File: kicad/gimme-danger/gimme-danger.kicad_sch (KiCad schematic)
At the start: 59 parts, among them J2 Barrel_Jack, J3 Screw_Terminal_01x06, Q1 AO3400A, Q2 AO3400A, Q3 AO3400A, Q4 AO3400A, U1 ESP32-S3-WROOM-1, U2 TPD6S300RUKR, U3 U261-241N-4BS2SS, U4 AO4407A, U5 SKRKAEE020, U6 DDTC143EUA, U7 SKRKAEE020, U8 TPS54302

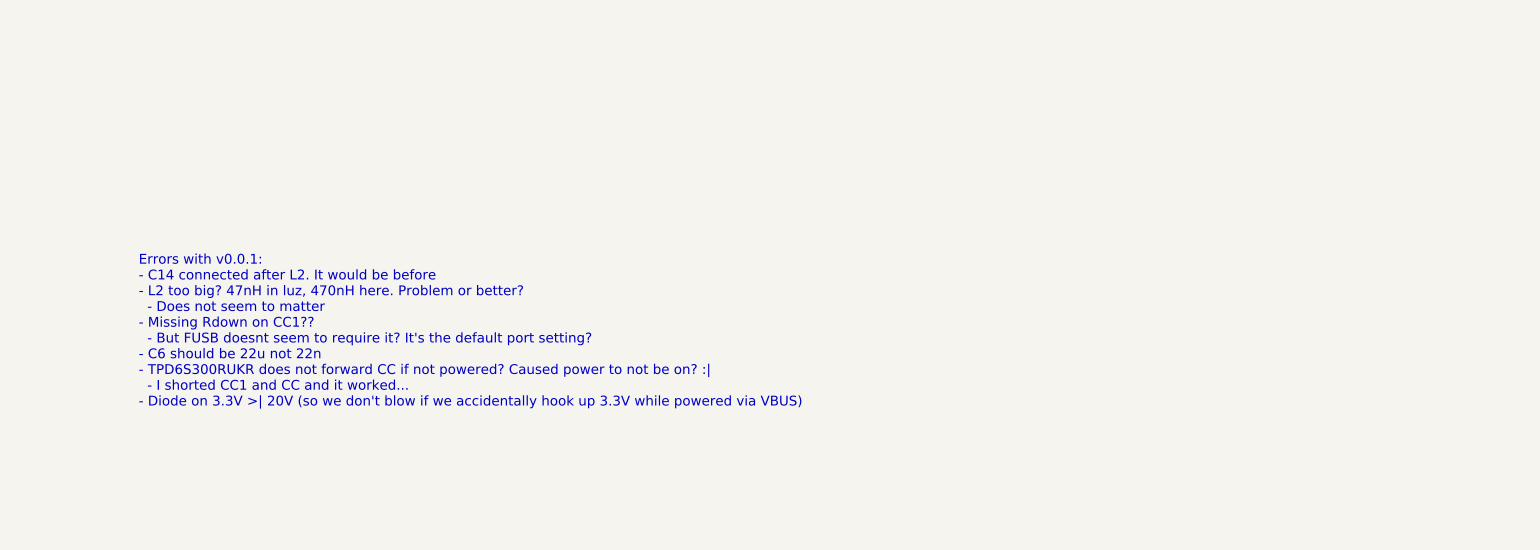
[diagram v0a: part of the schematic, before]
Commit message: YAML for 4 channels + wifi + fusb302
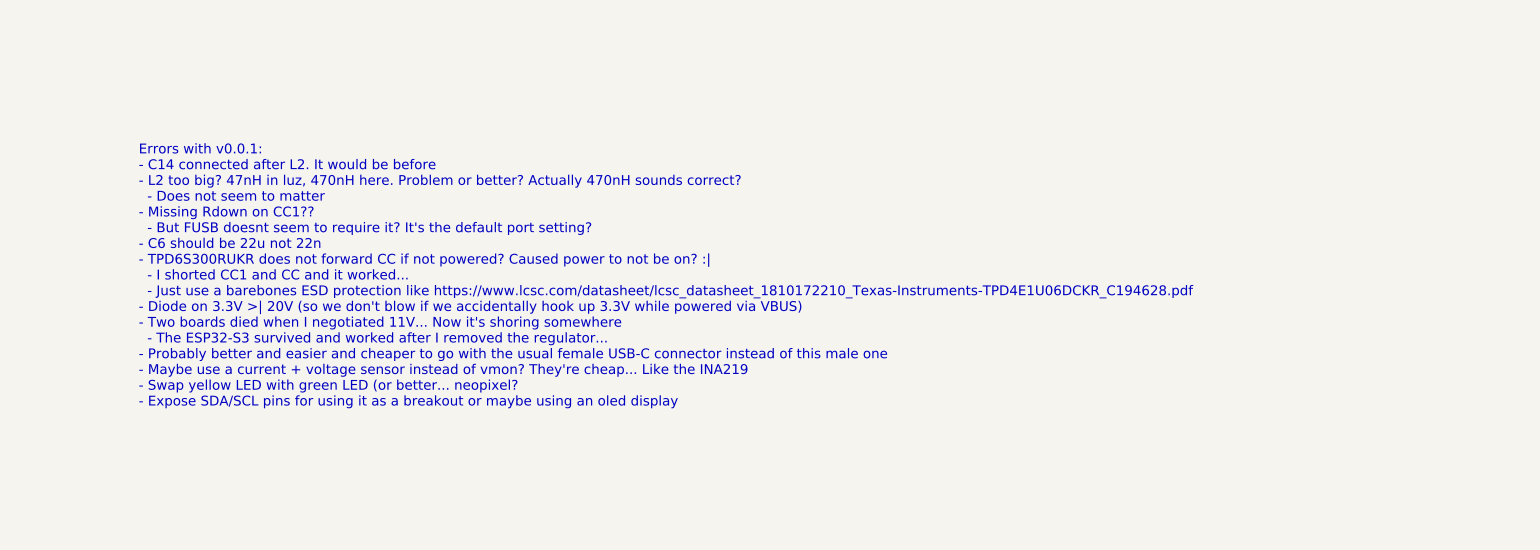
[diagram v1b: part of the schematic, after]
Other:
- note added: "Errors with v0.0.1: - C14 connected after L2. It would be before - L2 too big? 47nH in luz, 470nH here. Problem or better? Actually 470nH sounds correct? - Does not seem to matter - Missing Rdown on CC1?? - But FUSB doesnt seem to require it? It's the default port setting? - C6 should be 22u not 22n - TPD6S300RUKR does not forward CC if not powered? Caused power to not be on? :| - I shorted CC1 a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"
- note removed: "Errors with v0.0.1: - C14 connected after L2. It would be before - L2 too big? 47nH in luz, 470nH here. Problem or better? - Does not seem to matter - Missing Rdown on CC1?? - But FUSB doesnt seem to require it? It's the default port setting? - C6 should be 22u not 22n - TPD6S300RUKR does not forward CC if not powered? Caused power to not be on? :| - I shorted CC1 and CC and it worked... - Diode 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"
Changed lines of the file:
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@@
     (effects (font (size 1.27 1.27)) (justify left bottom))
   )
-  (text "Errors with v0.0.1:\n- C14 connected after L2. It would be before\n- L2 too big? 47nH in luz, 470nH here. Problem or better?\n  - Does not seem to matter\n- Missing Rdown on CC1??\n  - But FUSB doesnt seem to require it? It's the default port setting?\n- C6 should be 22u not 22n\n- TPD6S300RUKR does not forward CC if not powered? Caused power to not be on? :|\n  - I shorted CC1 and CC and it worked...\n- Diode on 3.3V >| 20V (so we don't blow if we accidentally hook up 3.3V while powered via VBUS)"
+  (text "Errors with v0.0.1:\n- C14 connected after L2. It would be before\n- L2 too big? 47nH in luz, 470nH here. Problem or better? Actually 470nH sounds correct?\n  - Does not seem to matter\n- Missing Rdown on CC1??\n  - But FUSB doesnt seem to require it? It's the default port setting?\n- C6 should be 22u not 22n\n- TPD6S300RUKR does not forward CC if not powered? Caused power to not be on? :|\n  - I shorted CC1 and CC and it worked...\n  - Just use a barebones ESD protection like https://www.lcsc.com/datasheet/lcsc_datasheet_1810172210_Texas-Instruments-TPD4E1U06DCKR_C194628.pdf\n- Diode on 3.3V >| 20V (so we don't blow if we accidentally hook up 3.3V while powered via VBUS)\n- Two boards died when I negotiated 11V... Now it's shoring somewhere\n  - The ESP32-S3 survived and worked after I removed the regulator...\n- Probably better and easier and cheaper to go with the usual female USB-C connector instead of this male one\n- Maybe use a current + voltage sensor instead of vmon? They're cheap... Like the INA219\n- Swap yellow LED with green LED (or better... neopixel?\n- Expose SDA/SCL pins for using it as a breakout or maybe using an oled display"
     (at 307.34 107.95 0)
     (effects (font (size 1.27 1.27)) (justify left bottom))

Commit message: New load switch design
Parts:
- removed C13: 0.1u, Capacitor_SMD:C_0402_1005Metric, symbol Device:C_Small
- removed R1, R7: 10k, Resistor_SMD:R_0402_1005Metric, symbol Device:R_Small
- removed R16: 1k, Resistor_SMD:R_0402_1005Metric, symbol Device:R_Small
- removed R8: 100k, Resistor_SMD:R_0402_1005Metric, symbol Device:R_Small
- removed U2: TPD6S300RUKR, footprint:WQFN-20_L3.0-W3.0-P0.40-BL-EP1.7, symbol TPD6S300RUKR:TPD6S300RUKR
- removed U3: U261-241N-4BS2SS, footprint:USB-C-SMD_U261-241N-4BS2SS, symbol U261-241N-4BS2SS:U261-241N-4BS2SS
- removed U4: AO4407A, footprint:SOIC-8_L4.9-W3.9-P1.27-LS6.0-BL, symbol AO4407A:AO4407A
- removed U6: DDTC143EUA, footprint:SOT-323-3_L2.0-W1.3-P1.30-LS2.1-BR, symbol DDTC143EUA-7-F:DDTC143EUA-7-F
- added D4: 18V, footprint:SOD-523_L1.2-W0.8-LS1.6-RD, symbol MM5Z18VT1G:MM5Z18VT1G
- added R22: 33k, Resistor_SMD:R_0402_1005Metric, symbol Device:R_Small
- added R23: 3.3k, Resistor_SMD:R_0402_1005Metric, symbol Device:R_Small
- added R24: 10m, footprint:R2512, symbol FMF25FPJR010-LHL:FMF25FPJR010-LHL
- added TP6, TP7, TP8: 3v3, TestPoint:TestPoint_Pad_D1.0mm, symbol Connector:TestPoint
- added U10: AO4805, footprint:SOIC-8_L4.9-W3.9-P1.27-LS6.0-BL, symbol AO4805:AO4805
- added U11: DDTC143EUA, footprint:SOT-323-3_L2.0-W1.3-P1.30-LS2.1-BR, symbol DDTC143EUA-7-F:DDTC143EUA-7-F
- added U2: TYPE-C-31-M-12, footprint:USB-C_SMD-TYPE-C-31-M-12, symbol TYPE-C-31-M-12:TYPE-C-31-M-12
- added U3: TPD4E1U06DCKR, footprint:SC-70-6_L2.2-W1.3-P0.65-LS2.1-BL, symbol TPD4E1U06DCKR:TPD4E1U06DCKR
- added U9: INA219AIDR, footprint:SOIC-8_L4.9-W3.9-P1.27-LS6.0-BL, symbol INA219AIDR:INA219AIDR
- C1: value 0.1u -> 1u; LCSC C307331 -> C52923
- C10, C9: value 1u -> 0.1u; LCSC C52923 -> C307331
- C6: value 22n -> 22u; footprint Capacitor_SMD:C_0402_1005Metric -> Capacitor_SMD:C_0805_2012Metric; LCSC C1532 -> C45783
- D1: footprint LED_SMD:LED_0603_1608Metric -> LED_SMD:LED_0805_2012Metric; LCSC C2286 -> C84256
- D2: footprint LED_SMD:LED_0603_1608Metric -> LED_SMD:LED_0805_2012Metric; LCSC C72038 -> C2297
- L2: value YNR6045-470M -> 47uH
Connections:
- net C_CC1 is gone; now on net CC1: TP5.1
- net +3V3: now also C10.2, U9.5 (VS); no longer C14.1, C9.1
- net CC1: now also U2.A5 (CC1), U3.6 (D1-)
- net D+: now also U2.A6 (DP1), U2.B6 (DP2), U3.3 (D2+)
- net D-: now also U2.A7 (DN1), U2.B7 (DN2), U3.1 (D1+)
- net GND: now also C10.1, U11.2 (GND(0)), U2.A1 (GND), U2.A12 (GND), U2.B1 (GND), U2.B12 (GND), U3.2 (GND), U9.1 (A1), U9.2 (A0), U9.6 (GND); no longer C10.2, C9.2
- net LOAD_EN#: now also U11.1 (IN)
- net SCL: now also TP8.1, U9.4 (SCL)
- net SDA: now also TP7.1, U9.3 (SDA)
- net VBUS: now also U10.5 (D1), U10.6 (D1), U2.A4 (VBUS), U2.A9 (VBUS), U2.B4 (VBUS), U2.B9 (VBUS)
- net VOUT: now also R24.2, U9.7 (VIN-); no longer C10.1
- net VSh+: now reaches C1.1
- net VSh+: now also R24.1, U10.7 (D2), U10.8 (D2), U9.8 (VIN+)
- net at L2.1, U8.2 (SW): now also C14.1
- net VMON: no longer names the net of U1.38 (GPIO2/TOUCH2/ADC1_CH1)
- new net: C9.2, D4.1 (K), R22.1, U10.1 (S2), U10.3 (S1)
- new net: C9.1, D4.2 (A), R22.2, R23.2, U10.2 (G2), U10.4 (G1)
- new net: R23.1, U11.3 (OUT)
- new net CC2: TP6.1, U2.B5 (CC2), U3.4 (D2-)
- no-connect marks 43 -> 33
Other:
- note added: "50V max"
- note added: "Addr 0x40"
- note added: "C9 - Slew rate RC ~0.3ms ON, ~3.3ms OFF D4 - Clamps max Vgs * For VBUS = 24V: * Iz ~ (24-18)/3.3k = 2mA; Pz = 18*2mA = 36mW * For VBUS = 48V: * Iz ~ (48-18)/3.3k = 10mA; Pz = 18*10mA = 180mW Reasoning: I'd eventually like to experiment with higher voltages. Most of this is not needed if we just care for max 20V."
- note added: "Current Sensor"
- note added: "ESD Protection"
- note added: "ESP32-S3"
- note added: "Errors with v0.0.1: - [DONE] C14 connected after L2. It would be before - [DONE] L2 too big? 47nH in luz, 470nH here. Problem or better? Actually 470nH sounds correct? - Does not seem to matter - [DONE] Missing Rdown on CC1?? - But FUSB doesnt seem to require it? It's the default port setting? - [DONE] C6 should be 22u not 22n - [DONE] TPD6S300RUKR does not forward CC if not powered? Caused power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"
- note added: "Terminals"
- note removed: "ESD, Short-to-VBUS Protection"
- note removed: "Errors with v0.0.1: - C14 connected after L2. It would be before - L2 too big? 47nH in luz, 470nH here. Problem or better? Actually 470nH sounds correct? - Does not seem to matter - Missing Rdown on CC1?? - But FUSB doesnt seem to require it? It's the default port setting? - C6 should be 22u not 22n - TPD6S300RUKR does not forward CC if not powered? Caused power to not be on? :| - I shorted CC1 a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"
- note removed: "UART"
- moved on the sheet: C12, C14, C15, C16, C2, C3, C4, C5, C6, C7, C8, D1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

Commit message: Notes
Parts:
- C1: footprint Capacitor_SMD:C_0402_1005Metric -> Capacitor_SMD:C_0603_1608Metric; LCSC C52923 -> C15849
- C4: footprint Capacitor_SMD:C_0603_1608Metric -> Capacitor_SMD:C_0805_2012Metric; LCSC C96446 -> C440198
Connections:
- net CC2: now also KEY1.1 (CC2), KEY1.14 (CC2)
- no-connect marks 33 -> 31
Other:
- note added: "C9 - Slew rate RC ~0.3ms ON, ~3.3ms OFF D4 - Clamps max Vgs * For VBUS = 24V: * Iz ~ (24-18)/3.3k = 2mA; Pz = 18*2mA = 36mW * For VBUS = 48V: * Iz ~ (48-18)/3.3k = 10mA; Pz = 18*10mA = 180mW Reasoning: I'd eventually like to experiment with higher voltages. Most of this is not needed if we just care for max 20V. Keep in mind that the MOSFETs are rated for 30V."
- note removed: "C9 - Slew rate RC ~0.3ms ON, ~3.3ms OFF D4 - Clamps max Vgs * For VBUS = 24V: * Iz ~ (24-18)/3.3k = 2mA; Pz = 18*2mA = 36mW * For VBUS = 48V: * Iz ~ (48-18)/3.3k = 10mA; Pz = 18*10mA = 180mW Reasoning: I'd eventually like to experiment with higher voltages. Most of this is not needed if we just care for max 20V."
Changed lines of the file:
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@@
   (no_connect (at 85.725 161.29))
   (no_connect (at 40.64 203.835))
-  (no_connect (at 313.055 95.885))
   (no_connect (at 43.18 203.835))
   (no_connect (at 281.94 149.225))
@@
   (no_connect (at 40.64 160.655))
   (no_connect (at 44.45 68.58))
-  (no_connect (at 287.655 95.885))
   (no_connect (at 135.89 116.84))
   (no_connect (at 135.89 81.28))
@@
     (stroke (width 0) (type default))
   )
-  (wire (pts (xy 313.055 93.345) (xy 316.865 93.345))
+  (wire (pts (xy 313.055 93.345) (xy 323.85 93.345))
     (stroke (width 0) (type default))
   )
@@
     (effects (font (size 1.27 1.27)) (justify left bottom))
   )
-  (text "Errors with v0.0.1:\n- [DONE] C14 connected after L2. It would be before\n- [DONE] L2 too big? 47nH in luz, 470nH here. Problem or better? Actually 470nH sounds correct?\n  - Does not seem to matter\n- [DONE] Missing Rdown on CC1??\n  - But FUSB doesnt seem to require it? It's the default port setting?\n- [DONE] C6 should be 22u not 22n\n- [DONE] TPD6S300RUKR does not forward CC if not powered? Caused power to not be on? :|\n  - I shorted CC1 and CC and it worked...\n  - Just use a barebones ESD protection like https://www.lcsc.com/datasheet/lcsc_datasheet_1810172210_Texas-Instruments-TPD4E1U06DCKR_C194628.pdf\n- Diode on 3.3V >| 20V (so we don't blow if we accidentally hook up 3.3V while powered via VBUS)\n- [??] Two boards died when I negotiated 11V... Now it's shoring somewhere\n  - The ESP32-S3 survived and worked after I removed the regulator...\n- [DONE] Probably better and easier and cheaper to go with the usual female USB-C connector instead of this male one\n- [DONE] Maybe use a current + voltage sensor instead of vmon? They're cheap... Like the INA219\n- [DONE] Swap yellow LED with green LED (or better... neopixel?\n- Expose SDA/SCL pins for using it as a breakout or maybe using an oled display\n- Test pad for both CC1 and CC2\n- Add disclaimer: max 20V, 5A\n- Mounting holes?\n- 20V Zener on load switching PChannel so we can possibly experiment with higher voltage on newer PD specs?"
+  (text "Errors with v0.0.1:\n- [DONE] C14 connected after L2. It would be before\n- [DONE] L2 too big? 47nH in luz, 470nH here. Problem or better? Actually 470nH sounds correct?\n  - Does not seem to matter\n- [DONE] Missing Rdown on CC1??\n  - But FUSB doesnt seem to require it? It's the default port setting?\n- [DONE] C6 should be 22u not 22n\n- [DONE] TPD6S300RUKR does not forward CC if not powered? Caused power to not be on? :|\n  - I shorted CC1 and CC and it worked...\n  - Just use a barebones ESD protection like https://www.lcsc.com/datasheet/lcsc_datasheet_1810172210_Texas-Instruments-TPD4E1U06DCKR_C194628.pdf\n- Diode on 3.3V >| 20V (so we don't blow if we accidentally hook up 3.3V while powered via VBUS)\n- [??] Two boards died when I negotiated 11V... Now it's shoring somewhere\n  - The ESP32-S3 survived and worked after I removed the regulator...\n- [DONE] Probably better and easier and cheaper to go with the usual female USB-C connector instead of this male one\n- [DONE] Maybe use a current + voltage sensor instead of vmon? They're cheap... Like the INA219\n- [DONE] Swap yellow LED with green LED (or better... neopixel?\n- Expose SDA/SCL pins for using it as a breakout or maybe using an oled display\n- Test pad for both CC1 and CC2\n- Add disclaimer: max 20V, 5A\n- Mounting holes?\n- [DONE] 20V Zener on load switching PChannel so we can possibly experiment with higher voltage on newer PD specs?\n- Double check capacitors rating - make sure > 50V\n- ESD protection on output"
     (at 433.705 201.295 0)
     (effects (font (size 1.27 1.27)) (justify left bottom))
@@
     (effects (font (size 1.27 1.27)) (justify left bottom))
   )
-  (text "C9 - Slew rate RC ~0.3ms ON, ~3.3ms OFF\nD4 - Clamps max Vgs\n  * For VBUS = 24V:\n    * Iz ~ (24-18)/3.3k = 2mA; Pz = 18*2mA = 36mW\n  * For VBUS = 48V:\n    * Iz ~ (48-18)/3.3k = 10mA; Pz = 18*10mA = 180mW\nReasoning: I'd eventually like to experiment with higher voltages.\nMost of this is not needed if we just care for max 20V."
+  (text "C9 - Slew rate RC ~0.3ms ON, ~3.3ms OFF\nD4 - Clamps max Vgs\n  * For VBUS = 24V:\n    * Iz ~ (24-18)/3.3k = 2mA; Pz = 18*2mA = 36mW\n  * For VBUS = 48V:\n    * Iz ~ (48-18)/3.3k = 10mA; Pz = 18*10mA = 180mW\nReasoning: I'd eventually like to experiment with higher voltages.\nMost of this is not needed if we just care for max 20V.\nKeep in mind that the MOSFETs are rated for 30V."
     (at 311.15 71.12 0)
     (effects (font (size 1.27 1.27)) (justify left bottom))
@@
     )
   )
+  (global_label "CC2" (shape input) (at 313.055 95.885 0) (fields_autoplaced)
+    (effects (font (size 1.27 1.27)) (justify left))
+    (property "Intersheetrefs" "${INTERSHEET_REFS}" (at 319.7103 95.885 0)
+      (effects (font (size 1.27 1.27)) (justify left) hide)
+    )
+  )
   (global_label "VOUT" (shape input) (at 328.295 31.75 0) (fields_autoplaced)
     (effects (font (size 1.27 1.27)) (justify left))
@@
     (effects (font (size 1.27 1.27)) (justify right))
     (property "Intersheetrefs" "${INTERSHEET_REFS}" (at 281.8463 106.045 0)
+      (effects (font (size 1.27 1.27)) (justify right) hide)
+    )
+  )
+  (global_label "CC2" (shape input) (at 287.655 95.885 180) (fields_autoplaced)
+    (effects (font (size 1.27 1.27)) (justify right))
+    (property "Intersheetrefs" "${INTERSHEET_REFS}" (at 280.9997 95.885 0)
       (effects (font (size 1.27 1.27)) (justify right) hide)
     )
@@
       (effects (font (size 1.27 1.27)) (justify left))
     )
-    (property "Footprint" "Capacitor_SMD:C_0603_1608Metric" (at 267.97 146.685 0)
+    (property "Footprint" "Capacitor_SMD:C_0805_2012Metric" (at 267.97 146.685 0)
       (effects (font (size 1.27 1.27)) hide)
     )
@@
       (effects (font (size 1.27 1.27)) hide)
     )
-    (property "LCSC" "C96446" (at 267.97 146.685 0)
+    (property "LCSC" "C440198" (at 267.97 146.685 0)
       (effects (font (size 1.27 1.27)) hide)
     )
@@
       (effects (font (size 1.27 1.27)) (justify left))
     )
-    (property "Value" "1u" (at 320.802 41.783 0)
-      (effects (font (size 1.27 1.27)) (justify left))
-    )
-    (property "Footprint" "Capacitor_SMD:C_0402_1005Metric" (at 314.96 42.545 0)
+    (property "Value" "1u" (at 321.31 41.275 0)
+      (effects (font (size 1.27 1.27)) (justify left))
+    )
+    (property "Footprint" "Capacitor_SMD:C_0603_1608Metric" (at 314.96 42.545 0)
       (effects (font (size 1.27 1.27)) hide)
     )
@@
       (effects (font (size 1.27 1.27)) hide)
     )
-    (property "LCSC" "C52923" (at 314.96 42.545 0)
+    (property "LCSC" "C15849" (at 314.96 42.545 0)
       (effects (font (size 1.27 1.27)) hide)
     )
@@
     )
   )
-  (symbol (lib_id "power:GND") (at 316.865 93.345 0) (unit 1)
-    (in_bom yes) (on_board yes) (dnp no)
-    (property "Reference" "#PWR015" (at 316.865 99.695 0)
-      (effects (font (size 1.27 1.27)) hide)
-    )
-    (property "Value" "GND" (at 320.675 95.25 0)
-      (effects (font (size 1.27 1.27)))
-    )
-    (property "Footprint" "" (at 316.865 93.345 0)
-      (effects (font (size 1.27 1.27)) hide)
-    )
-    (property "Datasheet" "" (at 316.865 93.345 0)
-      (effects (font (size 1.27 1.27)) hide)
-    )
+  (symbol (lib_id "power:GND") (at 323.85 93.345 0) (unit 1)
+    (in_bom yes) (on_board yes) (dnp no)
+    (property "Reference" "#PWR015" (at 323.85 99.695 0)
+      (effects (font (size 1.27 1.27)) hide)
+    )
+    (property "Value" "GND" (at 327.66 95.25 0)
+      (effects (font (size 1.27 1.27)))
+    )
+    (property "Footprint" "" (at 323.85 93.345 0)
+      (effects (font (size 1.27 1.27)) hide)
+    )
+    (property "Datasheet" "" (at 323.85 93.345 0)
+      (effects (font (size 1.27 1.27)) hide)
+    )

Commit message: TVS diodes on output
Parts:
- removed D3: 1N5819WS, Diode_SMD:D_SOD-323, symbol Diode:1N5819WS
- removed J2: Barrel_Jack, symbol Connector:Barrel_Jack
- removed U10: AO4805, footprint:SOIC-8_L4.9-W3.9-P1.27-LS6.0-BL, symbol AO4805:AO4805
- added D3, D5, D7, D8: SMAJ28A, footprint:SMA_L4.3-W2.6-LS5.2-RD, symbol SMAJ28A_C283899:SMAJ28A_C283899
- added D6: SMAJ48A, footprint:SMA_L4.3-W2.5-LS5.0-RD, symbol SMAJ48A_C353444:SMAJ48A_C353444
- added REF1, REF2: DMP6023LE-13, footprint:SOT-223-4_L6.5-W3.5-P2.30-LS7.0-BR, symbol DMP6023LE-13:DMP6023LE-13
- added U4: DC-84, footprint:DC-IN-TH_DC-84, symbol DC-84:DC-84
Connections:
- net GND: now also D6.2 (A), U4.2, U4.3
- net OUT1: now also D5.2
- net OUT2: now also D8.2
- net OUT3: now also D3.2
- net OUT4: now also D7.2
- net VBUS: now also REF1.2 (D), REF1.4 (D)
- net VOUT: now also D3.1, D5.1, D6.1 (C), D7.1, D8.1, U4.1
- net VSh+: now also REF2.2 (D), REF2.4 (D)
- net at C9.2, D4.1 (K), R22.1: now also REF1.3 (S), REF2.3 (S)
- net at C9.1, D4.2 (A), R22.2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: now also REF1.1 (G), REF2.1 (G)
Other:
- note added: "TODO - USB resistors (for termination + protection? 100 Ohm?) - [DONE] Voltage monitor? - [DONE] CC test pad - [DONE] Decoupling caps on CC line? How big? FUSB302 datasheet says 200 - 600 pF - [DONE] Make sure caps on VBUS/VINT support > 20V (what about surges?) - [DONE] TVS on VOUT -- eg. if we want to drive an inductive load with safety flyback? Maybe SMF22"
- note removed: "TODO - USB resistors (for termination + protection? 100 Ohm?) - [DONE] Voltage monitor? - [DONE] CC test pad - [DONE] Decoupling caps on CC line? How big? FUSB302 datasheet says 200 - 600 pF - Make sure caps on VBUS/VINT support > 20V (what about surges?) - TVS on VOUT -- eg. if we want to drive an inductive load with safety flyback? Maybe SMF22"
- moved on the sheet: C1, Q3, Q4, R17, R18, R24
